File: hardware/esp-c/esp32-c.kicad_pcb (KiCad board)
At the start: 2 copper layers, 70.5 x 64 mm, 76 parts, among them U1 MCP23008-E/ML, U10 HC-FPC-05-09-10RLTAG, U11 HC-FPC-05-09-10RLTAG, U12 ESP32-WROOM-32E(4MB), U13 AFC42-S14FMA-1H, U2 CH340C_C7464026, U3 SS8050_C2150, U4 MCP23008-E/ML, U5 MCP42010T-I/SL, U6 HC-FPC-05-09-10RLTAG, U7 IPFP051A30472R5, U8 SS8050_C2150, U9 AMS1117-3_3

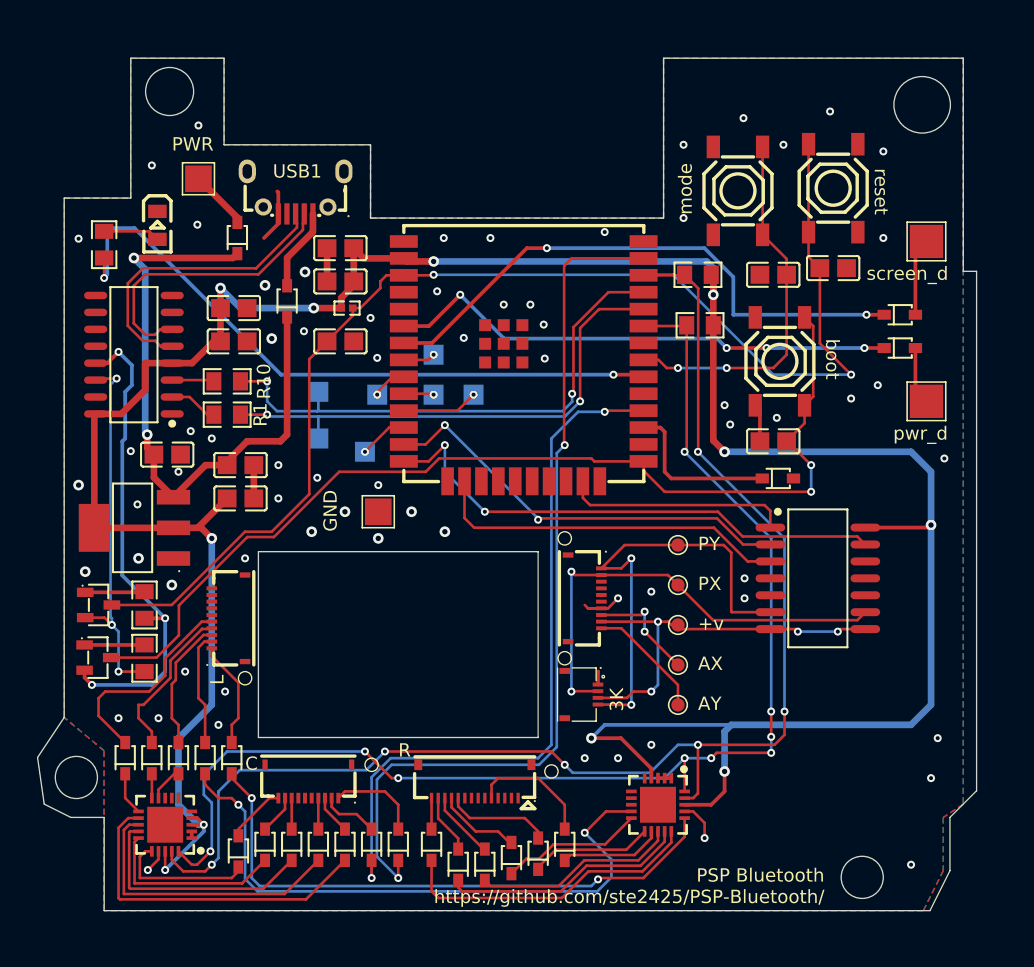
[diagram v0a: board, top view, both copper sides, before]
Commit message: Add 1K board connectors to board layout. Remove some unused pins from U13 footprint.
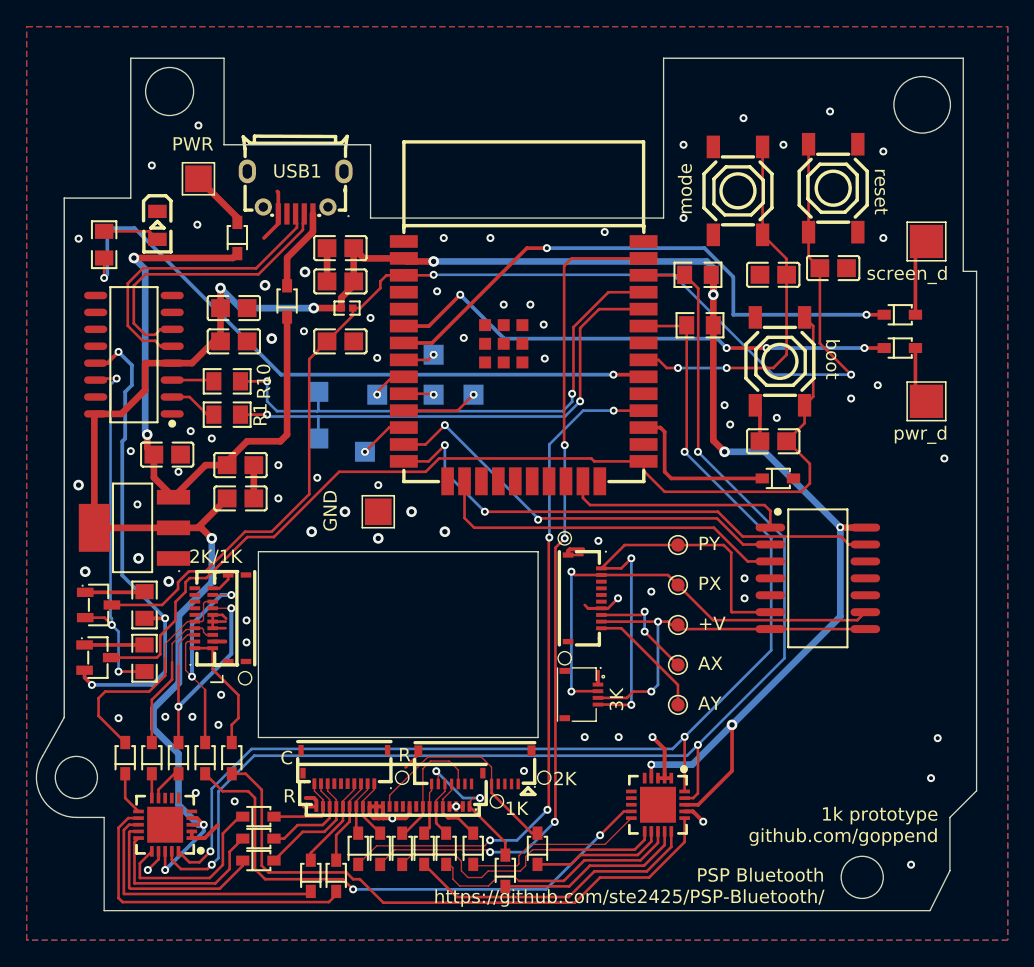
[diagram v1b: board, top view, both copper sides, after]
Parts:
- added U10-1k1: ~, JLCPCB_footprint:FPC-SMD_24P-P0.50_HC-FPC-05-09-24RLTAG, F.Cu at (129.1, 125.9)
- added U6-1k1: HC-FPC-05-09-10RLTAG, JLCPCB_footprint:FPC-SMD_10P-P0.50_HC-FPC-05-09-10RLTAG, F.Cu at (116.8, 113.0)
- moved D11 10.2 mm to (129.8, 130.3)
- moved D8 3.57 mm to (137.5, 132.0)
- moved D9 3.14 mm to (133.1, 130.3)
- moved D29 3.01 mm to (119.0, 127.9), turned to 0 degrees
- moved D10 2.96 mm to (135.1, 130.3)
- moved U10 2.91 mm to (125.5, 124.2)
- moved D27 2.77 mm to (119.0, 131.2), turned to 0 degrees
- moved D25 2.43 mm to (124.8, 132.3)
- moved D26 2.40 mm to (122.9, 132.3)
- moved D12 2.07 mm to (140.0, 130.3)
- moved D1 1.39 mm to (128.1, 130.3)
- moved U6 1.27 mm to (115.5, 113.0)
- moved U13 1.06 mm to (135.3, 124.2)
- moved D20 1.05 mm to (126.5, 130.3)
- moved D28 0.68 mm to (119.0, 129.5), turned to 0 degrees
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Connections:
- U7 pad 5: unconnected-(U7-Pad5) -> GND
- U7 pad 6: unconnected-(U7-Pad6) -> GND
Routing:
- net +3.3V: track 207.2 -> 176.4 mm
- net GND: track 23.4 -> 49.1 mm, vias 68 -> 75
- net cross: track 9.26 -> 21.9 mm
- net Net-(D3-A): track 8.77 -> 18.0 mm, vias 0 -> 2
- net Net-(D4-A): track 10.1 -> 19.3 mm, vias 0 -> 2
- net Net-(D12-A): track 9.36 -> 16.6 mm
- net Net-(D8-A): track 4.62 -> 11.4 mm, vias 0 -> 2
- net Net-(D27-A): track 2.61 -> 9.29 mm
- net ESP_I2C_SDA: track 94.9 -> 88.8 mm, vias 9 -> 3
- net right: track 46.4 -> 41.1 mm
- net Net-(D28-A): track 2.98 -> 8.03 mm
- net Net-(D26-A): track 2.61 -> 7.46 mm
- net ESP_I2C_SCL: track 101.1 -> 96.3 mm, vias 6 -> 3
- net r1: track 18.5 -> 14.3 mm
- net Net-(D25-A): track 2.95 -> 6.87 mm
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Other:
- board size 70.5 x 64 mm -> 70.6 x 64 mm
- board text added: "+V"
- board text added: "1K"
- board text added: "1k prototype github.com/goppend"
- board text added: "2K"
- board text added: "2K/1K"
- board text removed: "+v"

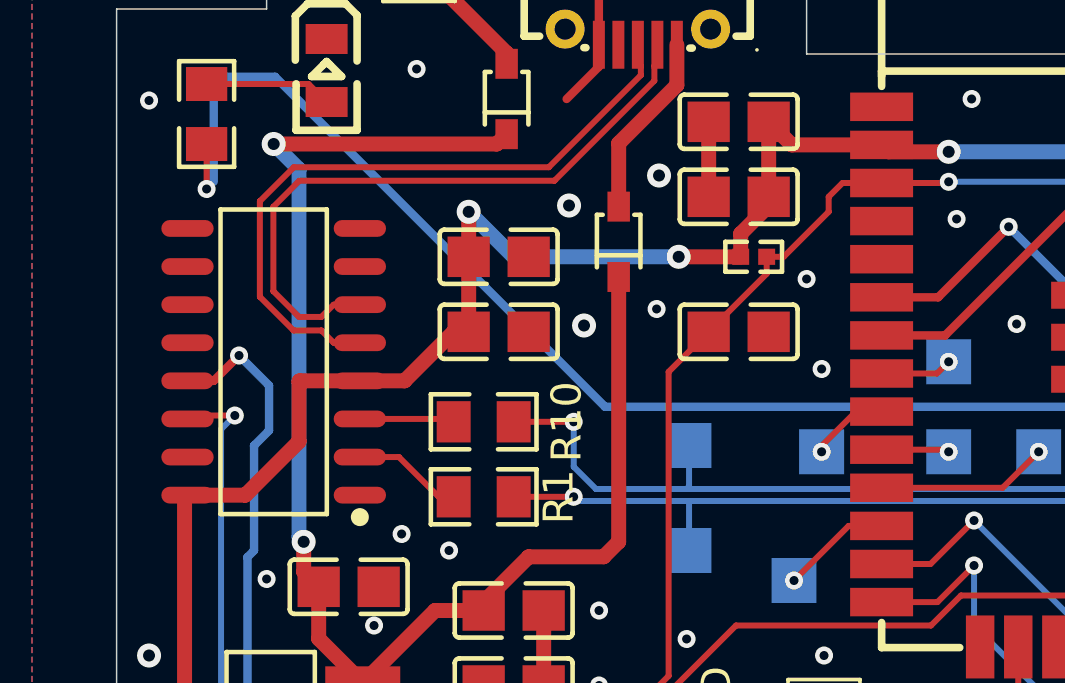
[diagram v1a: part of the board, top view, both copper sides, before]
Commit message: Update component R7 to use 0805 package instead of 0402. Tweak some associated traces.
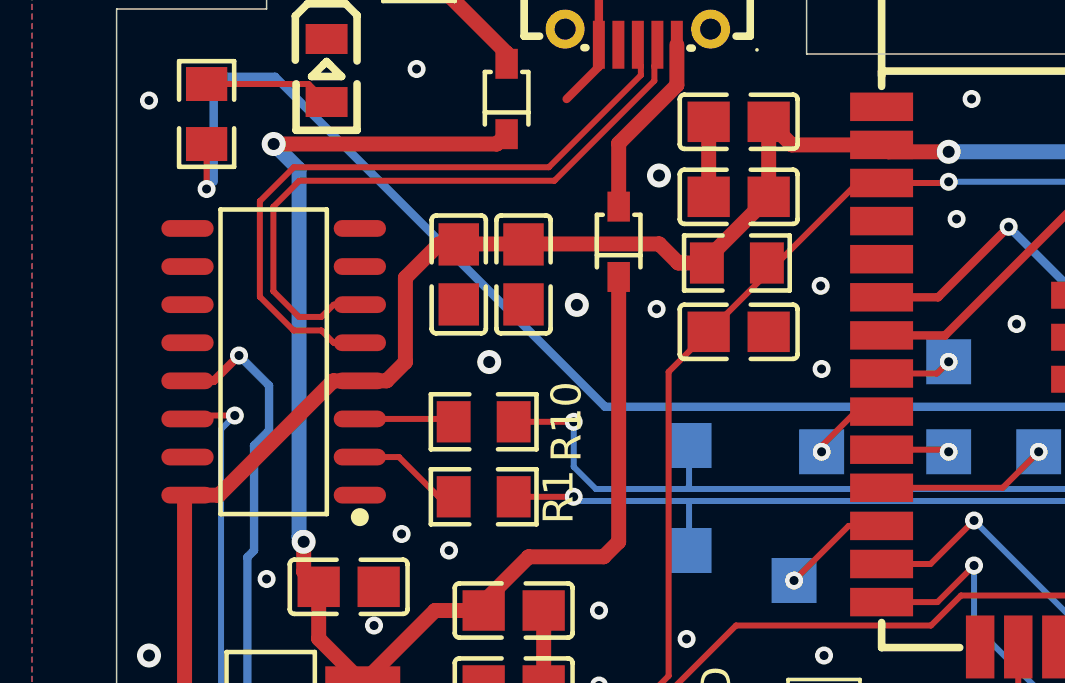
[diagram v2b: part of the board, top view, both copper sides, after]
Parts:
- R7: value 0402WGF1002TCE -> 0805W8F1002T5E; footprint JLCPCB_footprint:R0402 -> JLCPCB_footprint:R0805
- moved C5 2.08 mm to (118.0, 90.3), turned to 90 degrees
- moved C12 1.45 mm to (115.8, 90.3), turned to 90 degrees
- moved R7 0.60 mm to (125.1, 89.9)
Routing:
- net +3.3V: track 176.4 -> 172.8 mm, vias 11 -> 9
